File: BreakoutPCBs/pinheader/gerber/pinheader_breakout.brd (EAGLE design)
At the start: 25.5 x 25.4 mm, 2 parts

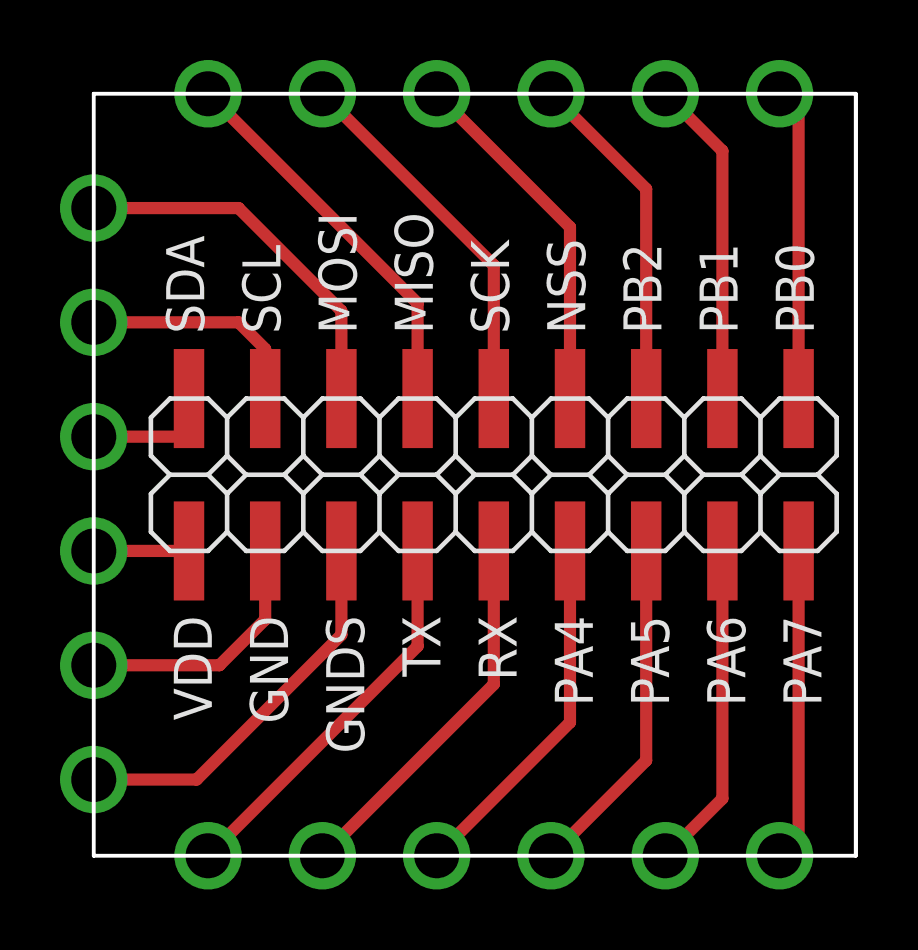
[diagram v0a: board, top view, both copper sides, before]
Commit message: update breakout pinheader
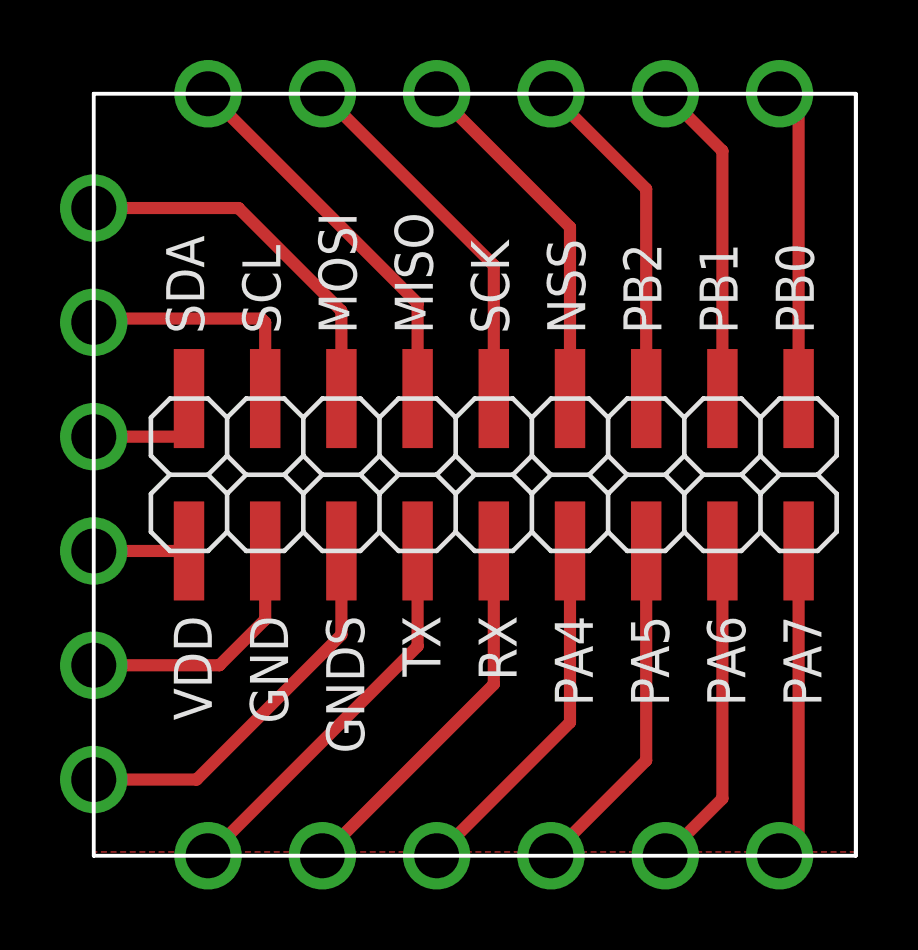
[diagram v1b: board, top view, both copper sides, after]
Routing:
- net SCL: track 7.73 -> 8.43 mm
- added copper zone on layer 1, net GND
- added copper zone on layer 16, net GND
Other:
- board text added: "Breakboard: SMD Pinheader Grid dim.: 2.54 mm"
- board text added: "github.com/NicoZellinger/ SensorMonitoring"
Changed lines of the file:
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@@
 <layer number="27" name="tValues" color="7" fill="1" visible="yes" active="yes"/>
 <layer number="28" name="bValues" color="7" fill="1" visible="yes" active="yes"/>
-<layer number="29" name="tStop" color="7" fill="3" visible="no" active="yes"/>
-<layer number="30" name="bStop" color="7" fill="6" visible="no" active="yes"/>
-<layer number="31" name="tCream" color="7" fill="4" visible="no" active="yes"/>
-<layer number="32" name="bCream" color="7" fill="5" visible="no" active="yes"/>
-<layer number="33" name="tFinish" color="6" fill="3" visible="no" active="yes"/>
-<layer number="34" name="bFinish" color="6" fill="6" visible="no" active="yes"/>
-<layer number="35" name="tGlue" color="7" fill="4" visible="no" active="yes"/>
-<layer number="36" name="bGlue" color="7" fill="5" visible="no" active="yes"/>
-<layer number="37" name="tTest" color="7" fill="1" visible="no" active="yes"/>
-<layer number="38" name="bTest" color="7" fill="1" visible="no" active="yes"/>
+<layer number="29" name="tStop" color="7" fill="3" visible="yes" active="yes"/>
+<layer number="30" name="bStop" color="7" fill="6" visible="yes" active="yes"/>
+<layer number="31" name="tCream" color="7" fill="4" visible="yes" active="yes"/>
+<layer number="32" name="bCream" color="7" fill="5" visible="yes" active="yes"/>
+<layer number="33" name="tFinish" color="6" fill="3" visible="yes" active="yes"/>
+<layer number="34" name="bFinish" color="6" fill="6" visible="yes" active="yes"/>
+<layer number="35" name="tGlue" color="7" fill="4" visible="yes" active="yes"/>
+<layer number="36" name="bGlue" color="7" fill="5" visible="yes" active="yes"/>
+<layer number="37" name="tTest" color="7" fill="1" visible="yes" active="yes"/>
+<layer number="38" name="bTest" color="7" fill="1" visible="yes" active="yes"/>
 <layer number="39" name="tKeepout" color="4" fill="11" visible="yes" active="yes"/>
 <layer number="40" name="bKeepout" color="1" fill="11" visible="yes" active="yes"/>
@@
 <layer number="42" name="bRestrict" color="1" fill="10" visible="yes" active="yes"/>
 <layer number="43" name="vRestrict" color="2" fill="10" visible="yes" active="yes"/>
-<layer number="44" name="Drills" color="7" fill="1" visible="no" active="yes"/>
-<layer number="45" name="Holes" color="7" fill="1" visible="no" active="yes"/>
-<layer number="46" name="Milling" color="3" fill="1" visible="no" active="yes"/>
-<layer number="47" name="Measures" color="7" fill="1" visible="no" active="yes"/>
+<layer number="44" name="Drills" color="7" fill="1" visible="yes" active="yes"/>
+<layer number="45" name="Holes" color="7" fill="1" visible="yes" active="yes"/>
+<layer number="46" name="Milling" color="3" fill="1" visible="yes" active="yes"/>
+<layer number="47" name="Measures" color="7" fill="1" visible="yes" active="yes"/>
 <layer number="48" name="Document" color="7" fill="1" visible="yes" active="yes"/>
 <layer number="49" name="Reference" color="7" fill="1" visible="yes" active="yes"/>
@@
 <text x="24.003" y="17.399" size="1.27" layer="25" rot="R90">PB0</text>
 <text x="21.463" y="17.399" size="1.27" layer="25" rot="R90">PB1</text>
+<text x="23.114" y="19.431" size="1.016" layer="26" font="vector" rot="MR0">github.com/NicoZellinger/
+SensorMonitoring</text>
+<text x="23.241" y="3.048" size="1.016" layer="26" font="vector" rot="MR0">Breakboard:
+SMD Pinheader
+Grid dim.: 2.54 mm</text>
 </plain>
 <attributes>
@@
 <wire x1="5.715" y1="7.874" x2="4.191" y2="6.35" width="0.4064" layer="1"/>
 <wire x1="4.191" y1="6.35" x2="0" y2="6.35" width="0.4064" layer="1"/>
+<polygon width="0.4064" layer="1">
+<vertex x="0" y="25.4"/>
+<vertex x="25.4" y="25.4"/>
+<vertex x="25.4" y="0.127"/>
+<vertex x="0" y="0.127"/>
+</polygon>
+<polygon width="0.4064" layer="16">
+<vertex x="0" y="25.4"/>
+<vertex x="25.4" y="25.4"/>
+<vertex x="25.4" y="0"/>
+<vertex x="0" y="0"/>
+</polygon>
 </signal>
 <signal name="GNDIO">
@@
 <contactref element="U$1" pad="P$14"/>
 <contactref element="JP1" pad="4"/>
-<wire x1="5.715" y1="15.24" x2="5.715" y2="16.891" width="0.4064" layer="1"/>
-<wire x1="5.715" y1="16.891" x2="4.826" y2="17.78" width="0.4064" layer="1"/>
-<wire x1="4.826" y1="17.78" x2="0" y2="17.78" width="0.4064" layer="1"/>
+<wire x1="5.715" y1="15.24" x2="5.715" y2="17.78" width="0.4064" layer="1"/>
+<wire x1="5.715" y1="17.78" x2="5.588" y2="17.907" width="0.4064" layer="1"/>
+<wire x1="5.588" y1="17.907" x2="0" y2="17.907" width="0.4064" layer="1"/>
+<wire x1="0" y1="17.907" x2="0" y2="17.78" width="0.4064" layer="1"/>
 </signal>
 <signal name="SDA">
@@
 </board>
 </drawing>
+<compatibility>
+<note version="6.3" minversion="6.2.2" severity="warning">
+Since Version 6.2.2 text objects can contain more than one line,
+which will not be processed correctly with this version.
+</note>
+</compatibility>
 </eagle>
